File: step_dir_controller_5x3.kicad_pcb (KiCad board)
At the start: 2 copper layers, 121.3 x 67.3 mm, 1 part

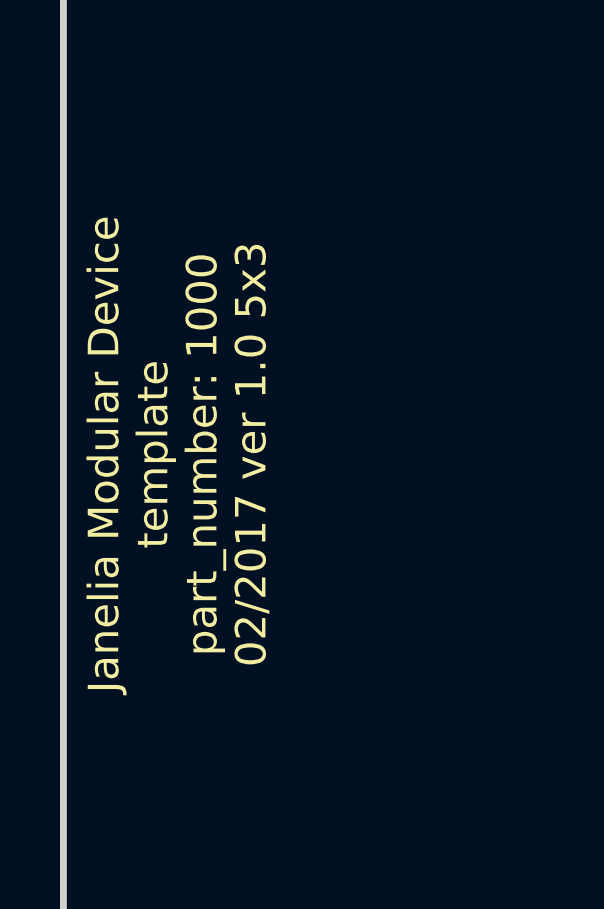
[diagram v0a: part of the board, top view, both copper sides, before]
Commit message: template -> step_dir_controller.
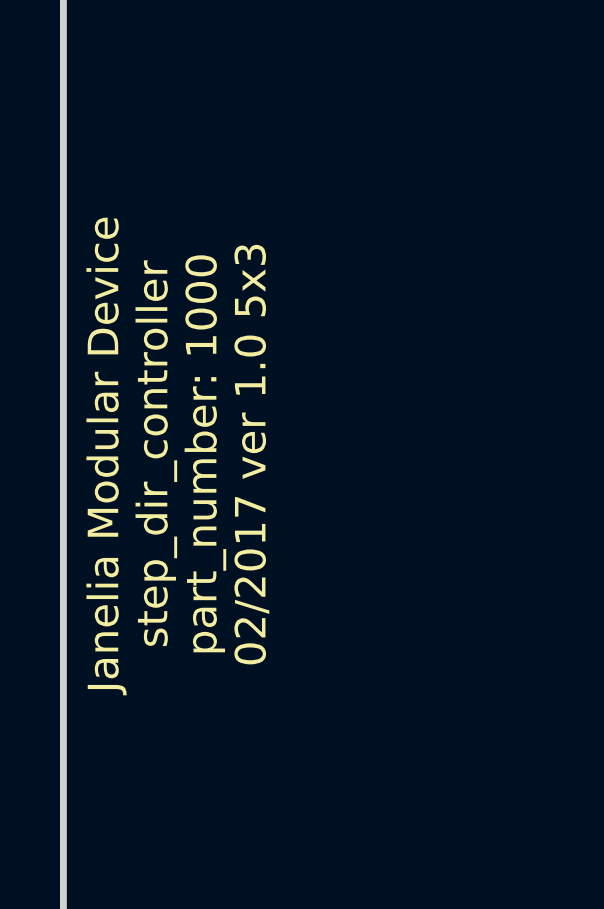
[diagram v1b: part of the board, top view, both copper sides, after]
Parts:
- MDB1: footprint template_5x3:MODULAR_DEVICE_BASE_5X3_MALE -> step_dir_controller_5x3:MODULAR_DEVICE_BASE_5X3_MALE
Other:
- board text added: "Janelia Modular Device step_dir_controller part_number: 1000 02/2017 ver 1.0 5x3"
- board text removed: "Janelia Modular Device template part_number: 1000 02/2017 ver 1.0 5x3"
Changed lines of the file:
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@@
   (page A4)
   (title_block
-    (title template_5x3)
+    (title step_dir_controller_5x3)
     (rev 1.0)
   )
@@
     (diff_pair_width 0.254)
   )
-  (module template_5x3:MODULAR_DEVICE_BASE_5X3_MALE (layer F.Cu)
+  (module step_dir_controller_5x3:MODULAR_DEVICE_BASE_5X3_MALE (layer F.Cu)
     (at 91.44 105.41)
     (fp_text reference MDB1 (at 0 0) (layer F.SilkS) hide
@@
     (effects (font (size 1.016 1.016) (thickness 0.1905)))
   )
-  (gr_text "Janelia Modular Device\ntemplate\npart_number: 1000\n02/2017 ver 1.0 5x3" (at 73.66 105.41 90) (layer F.SilkS)
+  (gr_text "Janelia Modular Device\nstep_dir_controller\npart_number: 1000\n02/2017 ver 1.0 5x3" (at 73.66 105.41 90) (layer F.SilkS)
     (effects (font (size 1.016 1.016) (thickness 0.254)))
   )
